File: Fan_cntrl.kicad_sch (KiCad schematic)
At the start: 17 parts, among them J10 61900411021, J7 61900411021, J8 61900411021, J9 61900411021, U29 EMC2305

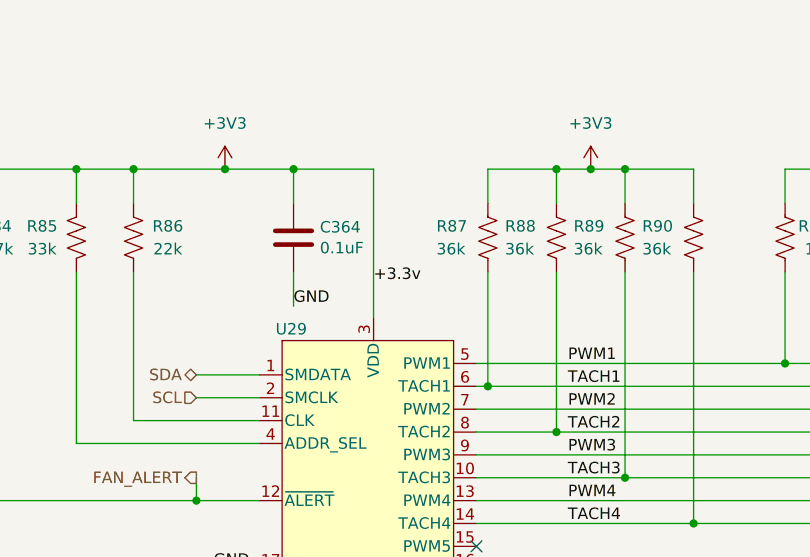
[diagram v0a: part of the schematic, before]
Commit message: board stakup updated and schematic is updated
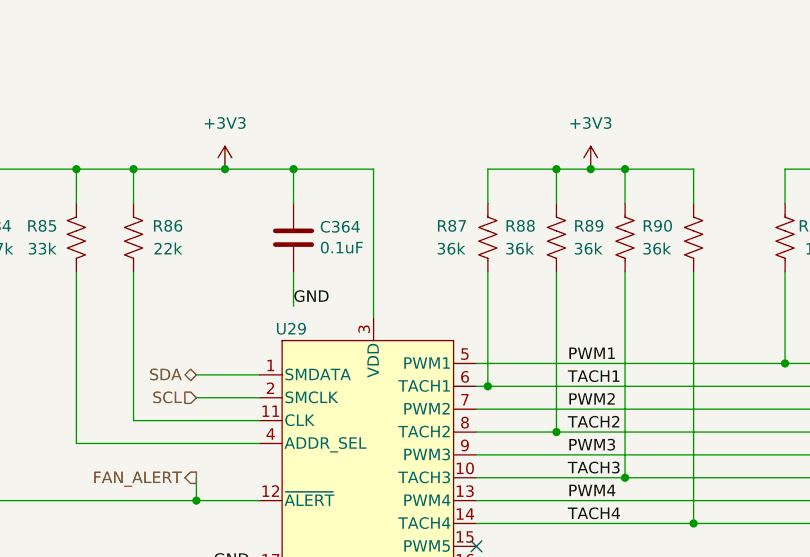
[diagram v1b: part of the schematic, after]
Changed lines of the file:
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@@
-		)
-	)
-	(label "+3.3v"
-		(at 99.695 69.215 0)
-		(effects
-			(font
-				(size 1.27 1.27)
-			)
-			(justify left bottom)
 		)
 	)

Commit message: updated schematic working on layout
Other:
- company: (none) -> Author: Aadhi M
- title: (none) -> PC-AXE
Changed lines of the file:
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@@
 	(generator_version "9.0")
 	(paper "A4")
+	(title_block
+		(title "PC-AXE")
+		(company "Author: Aadhi M")
+	)
 	(text "I2C Address: 0x4D"
 		(exclude_from_sim no)
